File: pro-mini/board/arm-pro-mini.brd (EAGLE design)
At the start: 38.1 x 20.3 mm, 57 parts, among them J1 USB, J2 SWD HEADER, Q1 12Mhz, T1 DTA114EET1G (2 X 10K), U1 MCP1754ST-3302E/CB, U2 NUF2042XV6T1G, U3 LPC11U35FHI33/501

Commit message: Bumped version number to 3. Tweaked labels.
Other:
- board text added: "REV 3"
- board text removed: "REV 2F"
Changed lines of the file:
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@@
 MINI
 PRO</text>
-<text x="21.717" y="4.191" size="0.762" layer="21" font="vector" ratio="10">REV 2F</text>
+<text x="21.717" y="4.191" size="0.762" layer="21" font="vector" ratio="10">REV 3</text>
 <wire x1="1.27" y1="2.413" x2="1.27" y2="2.159" width="0.1524" layer="21"/>
 <wire x1="11.43" y1="2.413" x2="11.43" y2="2.159" width="0.1524" layer="21"/>
@@
 </element>
 <element name="C2" library="arm-pro-mini" package="C0603K" value="1u" x="10.459640625" y="11.380425" smashed="yes" rot="R180">
-<attribute name="NAME" x="7.576840625" y="11.293825" size="0.762" layer="25" font="vector" ratio="10"/>
+<attribute name="NAME" x="11.005840625" y="9.896825" size="0.762" layer="25" font="vector" ratio="10"/>
 <attribute name="VALUE" x="11.259640625" y="13.030425" size="1.016" layer="27" rot="R180"/>
 </element>
@@
 </element>
 <element name="C4" library="arm-pro-mini" package="C0402K" value="18pF" x="17.907" y="14.4018" smashed="yes" rot="R90">
-<attribute name="NAME" x="17.4672" y="15.831" size="0.762" layer="25" font="vector" ratio="10" rot="R180"/>
+<attribute name="NAME" x="18.2292" y="16.466" size="0.762" layer="25" font="vector" ratio="10" rot="R180"/>
 <attribute name="VALUE" x="19.357" y="13.9018" size="1.016" layer="27" rot="R90"/>
 </element>
 <element name="C6" library="arm-pro-mini" package="C0603K" value="0.1uF" x="23.8506" y="7.1882" smashed="yes">
-<attribute name="NAME" x="24.0156" y="6.3858" size="0.762" layer="25" font="vector" ratio="10" rot="R180"/>
+<attribute name="NAME" x="25.2856" y="8.9258" size="0.762" layer="25" font="vector" ratio="10" rot="R180"/>
 <attribute name="VALUE" x="23.0506" y="5.5382" size="1.016" layer="27"/>
 </element>

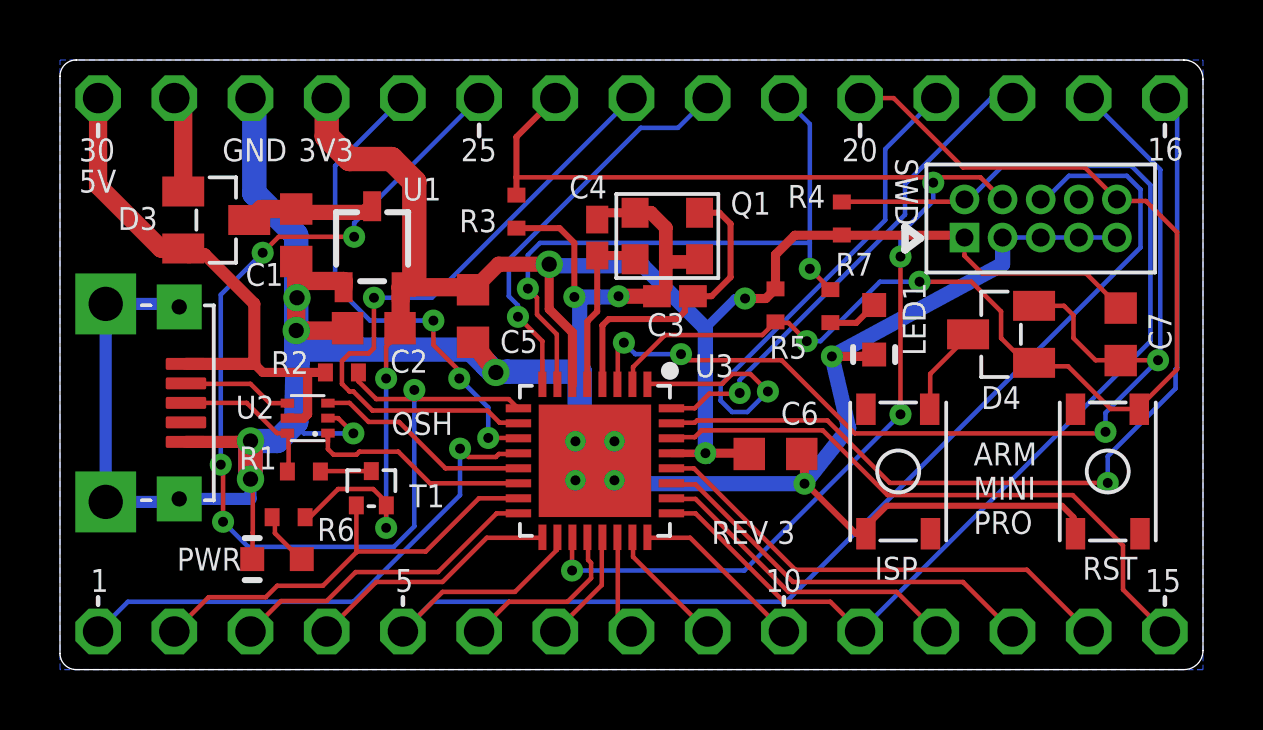
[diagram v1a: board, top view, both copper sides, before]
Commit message: Minor tweaking of components' locations. Made the LED more visible behind the button.
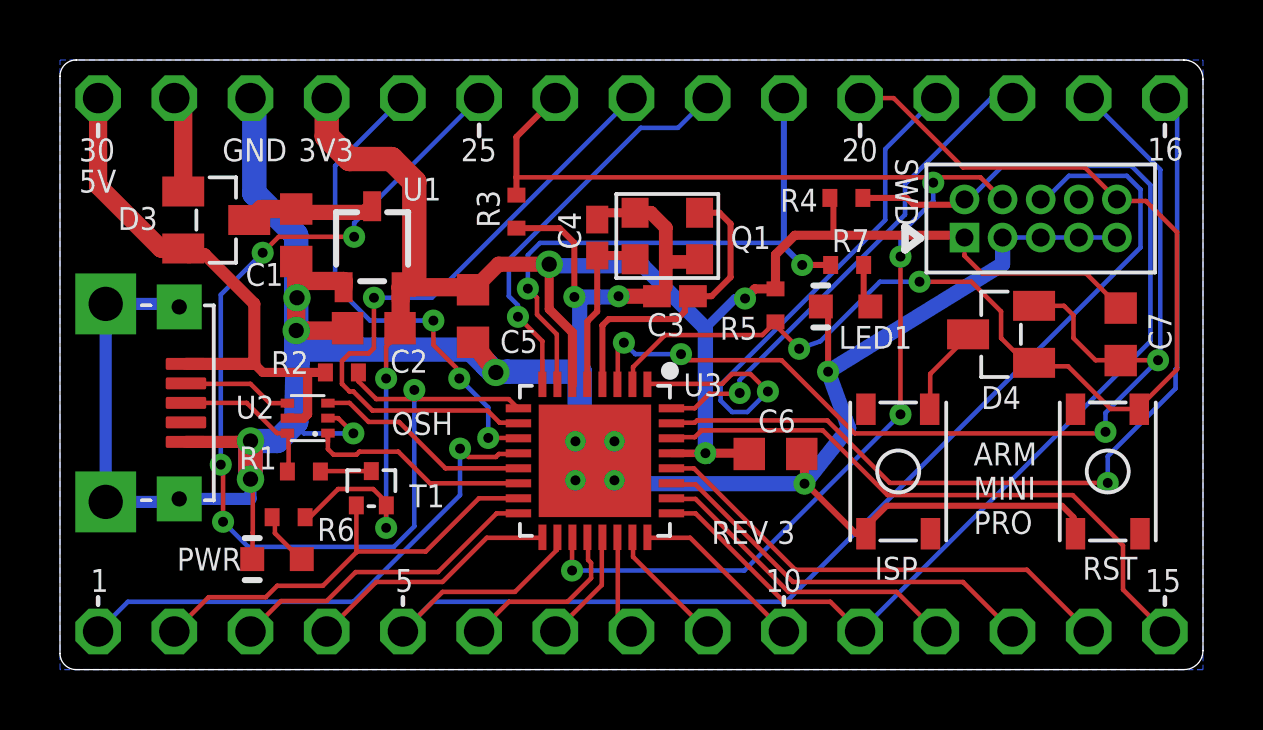
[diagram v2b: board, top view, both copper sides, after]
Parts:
- moved R7 1.48 mm to (26.2, 13.5), turned to 180 degrees
- moved D1 1.23 mm to (26.2, 12.1), turned to 90 degrees
- moved R4 0.70 mm to (26.2, 15.7), turned to 180 degrees
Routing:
- net +3V3: track 62.6 -> 63.9 mm
- net PIO0_20-LED1: track 21.3 -> 20.4 mm
- net GND: track 120.2 -> 120.9 mm
- net PIO0_15-SWDIO: track 37.9 -> 37.3 mm
